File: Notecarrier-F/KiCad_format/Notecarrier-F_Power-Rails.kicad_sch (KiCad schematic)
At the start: 28 parts, among them U10 TPS63020DSJR, U11 MAX17225ELT+, U9 TPS62748YFPT

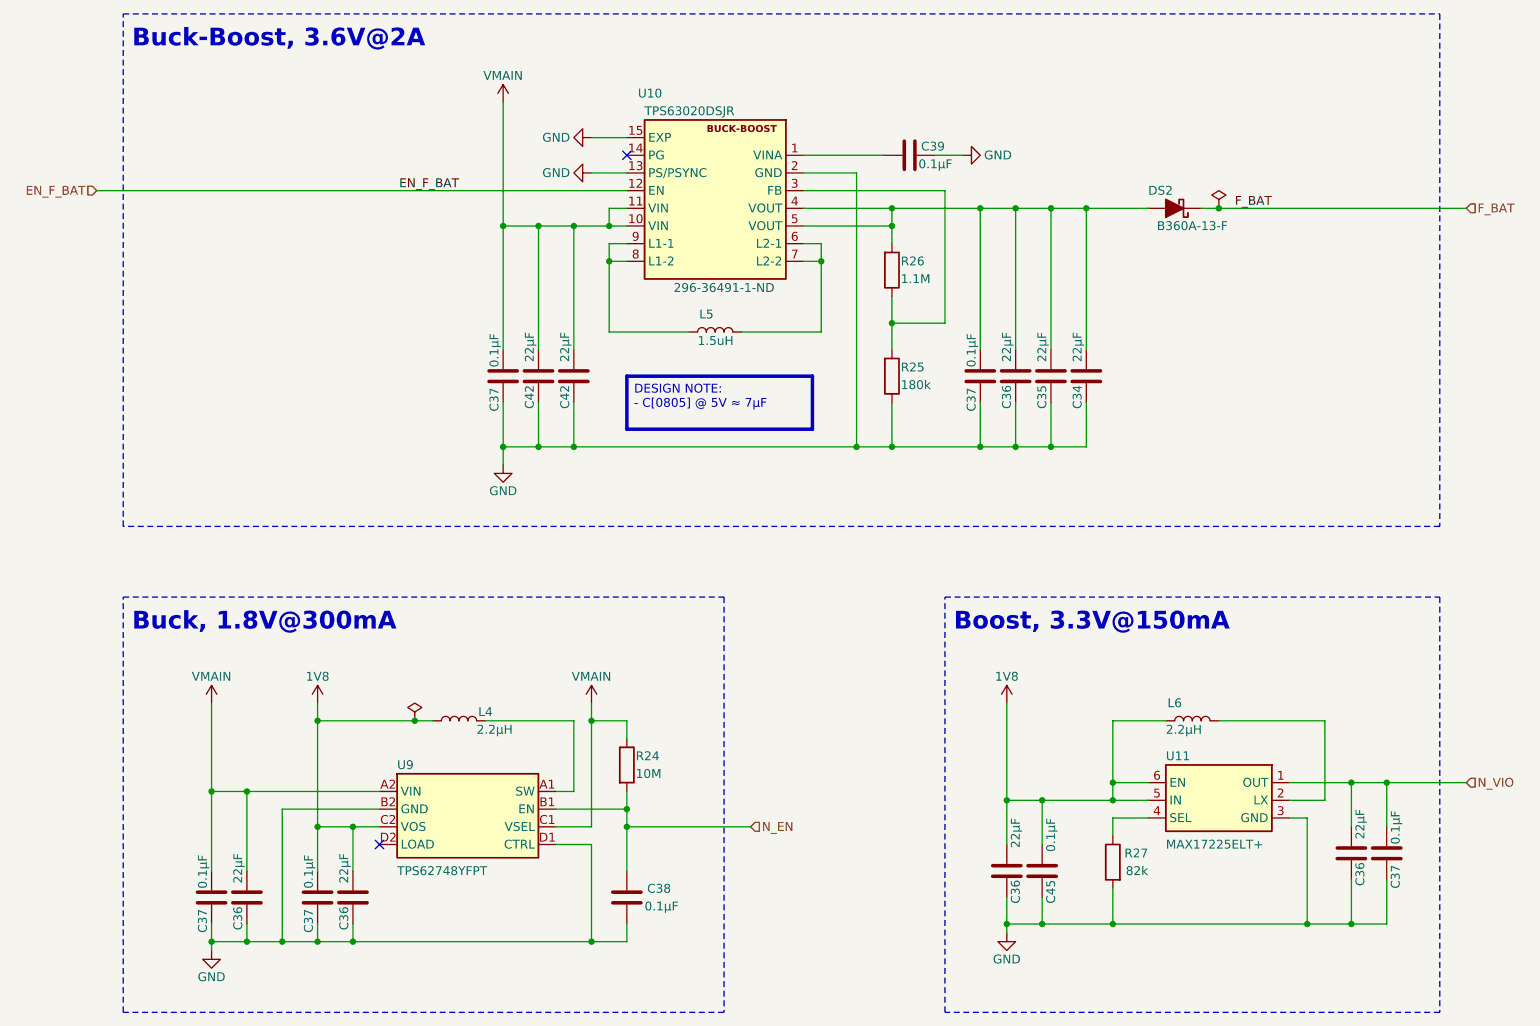
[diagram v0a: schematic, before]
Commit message: Complete first pass PCB rev B.
See README for details. Ready to start Validation.
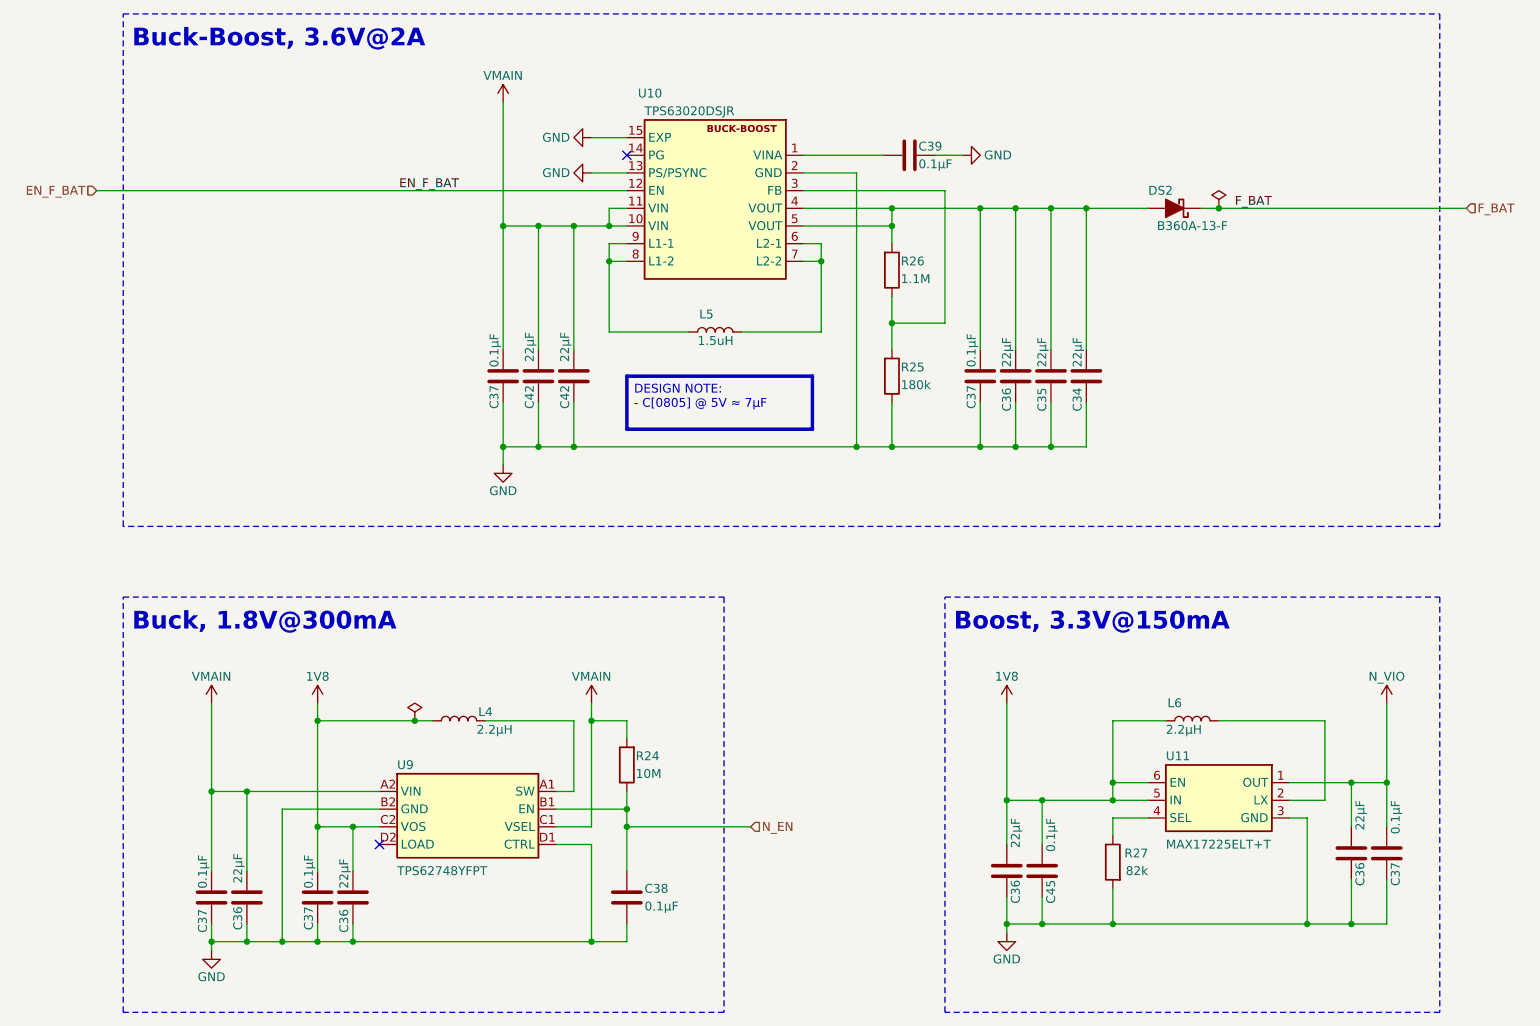
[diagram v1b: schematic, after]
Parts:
- C34, C35, C36: footprint blues-kicad-lib:CAP FILM 0805 -> blues-kicad-lib:C-0805_Fv1.2; Design Description (none) -> Capacitor ceramic 22u ±10% X5R 16V 0805; Design MPN (none) -> N/A; Design Manufacturer (none) -> N/A; MPN (none) -> CL21A226MOQNNNE; Mfr Description (none) -> Cap Ceramic 22uF 16V X5R 20% SMD 0805 85°C Embossed Plastic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; Order Code CL21A226MOQNNNE -> (none); Part Number CL21A226MOQNNNE -> (none); Supplier Avnet -> (none)
- C37, C38, C39, C45: footprint blues-kicad-lib:CAP 0402_1005 -> blues-kicad-lib:C-0402_Fv1.2; Datasheet 2 (none) -> http://datasheet.octopart.com/CL05B104KO5NNNC-Samsung-Elect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; Datasheet 3 (none) -> https://datasheet.octopart.com/GRM155R71C104KA88D-Murata-da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; Design Description (none) -> Capacitor ceramic 100n ±10% X7R 16V 0402; Design MPN (none) -> N/A; Design Manufacturer (none) -> N/A; Design Order Code (none) -> 490-3261-1-ND; Design Supplier (none) -> Digi-Key; MPN (none) -> CC0402KRX7R7BB104; MPN 2 (none) -> CL05B104KO5NNNC; MPN 3 (none) -> GRM155R71C104KA88D; Manufacturer Samsung -> Yageo; Manufacturer 2 (none) -> Samsung; Manufacturer 3 (none) -> Murata; Mfr Description (none) -> 0402 0.1 uF 16 V ±10 % Tolerance X7R SMT Multilayer Ceramic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; Mfr Description 2 (none) -> Ceramic capacitor SMD-0402 100nF /16V X7R# K +-10%, Samsung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; Mfr Description 3 (none) -> Multilayer Ceramic Capacitor, 0.1 uF, 16 V, ± 10%, X7R, 040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; Order Code 187-CL05B104KO5NNNC -> (none); Part Number CL05B104KO5NNNC -> (none); Supplier Farnell -> (none)
- C42: footprint blues-kicad-lib:CAP 0603_1608 -> blues-kicad-lib:C-0805_Fv1.2; Design Description (none) -> Capacitor ceramic 22u ±10% X5R 16V 0805; Design MPN (none) -> N/A; Design Manufacturer (none) -> N/A; MPN (none) -> CL21A226MOQNNNE; Manufacturer (none) -> Samsung; Mfr Description (none) -> Cap Ceramic 22uF 16V X5R 20% SMD 0805 85°C Embossed Plastic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
- DS2: footprint (none) -> blues-kicad-lib:DO-214AC SMA_Fv1.2; symbol Device:D_Schottky_Filled -> blues-kicad-lib:D_Schottky_Filled_Swapped; Design Description (none) -> Schottky Diode B360-13-F 60V/3A; Design MPN (none) -> B360A-13-F; Design Manufacturer (none) -> Diodes Inc; Design Order Code (none) -> B360A-FDICT-ND; Design Supplier (none) -> Digi-Key; MPN (none) -> B360A-13-F; Manufacturer (none) -> Diodes Inc.; Mfr Description (none) -> Rectifier Diode, Schottky, 1 Phase, 1 Element, 3A, 60V V(RR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
- L4: footprint blues-kicad-lib:1285AS-H-2R2M=P2-INDC2016X100N -> blues-kicad-lib:1285AS-H-2R2M=P2-INDC2016X100N_Fv1.2; Design Description (none) -> FIXED IND 2.2UH 1.5A 204MOHM SMD; Design MPN (none) -> 1285AS-H-2R2M=P2; Design Manufacturer (none) -> Murata Electronics; Design Order Code (none) -> 490-10600-1-ND; Design Supplier (none) -> Digi-Key; MPN (none) -> 1285AS-H-2R2M=P2; Mfr Description (none) -> 2.2µH Shielded Wirewound Inductor 1.5A 204mOhm Max 0805 (20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; Order Code 490-10600-1-ND -> (none); Part Number 1285AS-H-2R2M=P2 -> (none); Supplier Digi-Key -> (none)
- L5: footprint blues-kicad-lib:VCHA042A-1R5MS6 -> blues-kicad-lib:VCHA042A-1R5MS6_Fv1.2; Design Description (none) -> Fixed Ind 1.5UH 7.3A 15.4 Mohm; Design MPN (none) -> VCHA042A-1R5MS6; Design Manufacturer (none) -> Cyntec; Design Order Code (none) -> 2037-VCHA042A-1R5MS6CT-ND; Design Supplier (none) -> Digi-Key; MPN (none) -> VCHA042A-1R5MS6; Mfr Description (none) -> Fixed Ind 1.5UH 7.3A 15.4MOHM Sm; Order Code 2037-VCHA042A-1R5MS6CT-ND -> (none); Part Number VCHA042A-1R5MS6 -> (none); Supplier Digi-Key -> (none)
- L6: footprint blues-kicad-lib:IND_XFL4020-222MEC -> blues-kicad-lib:IND_XFL4020-222MEC_Fv1.2; Design Description (none) -> Power Inductors - SMD 2.2Uh Shld 8A 23.5mOhms AECQ2; Design MPN (none) -> XFL4020-222MEC; Design Manufacturer (none) -> Coilcraft; Design Order Code (none) -> 994-XFL4020-222MEC; Design Supplier (none) -> Mouser; MPN (none) -> XFL4020-222MEC; Mfr Description (none) -> Inductor Power Shielded Wirewound 2.2uH 20% 1MHz 8A 0.0235O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; Order Code XFL4020-222MEC -> (none); Part Number XFL4020-222MEC -> (none)
- R24: footprint blues-kicad-lib:RES 0402_1005 -> blues-kicad-lib:R-0402_Fv1.2; Datasheet 2 (none) -> https://datasheet.octopart.com/AC0402FR-0710ML-Yageo-datash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; Design Description (none) -> Resistor 10M ±1% 0402; Design MPN (none) -> N/A; Design Manufacturer (none) -> N/A; Design Order Code (none) -> RC0402FR-0710ML; Design Supplier (none) -> Digi-Key; MPN (none) -> RC0402FR-0710ML; MPN 2 (none) -> AC0402FR-0710ML; Manufacturer 2 (none) -> Yageo; Mfr Description (none) -> Res General Purpose Thick Film 0402 10M Ohm 1% 1/16W ±100pp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; Mfr Description 2 (none) -> Res Thick Film 0402 10M Ohm 1% 0.063W(1/16W) ±100ppm/C Pad 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; Order Code 311-10MJRCT-ND -> (none); Part Number RC0402JR-0710ML -> (none); Supplier Digi-Key -> (none)
- R25: footprint blues-kicad-lib:RES 0402_1005 -> blues-kicad-lib:R-0402_Fv1.2; Design Description (none) -> Resistor 180k ±1% 0402; Design MPN (none) -> N/A; Design Manufacturer (none) -> N/A; MPN (none) -> RC0402FR-07180KL; Mfr Description (none) -> Res Thick Film 0402 180K Ohm 1% 1/16W +/-100ppm/ßC Molded S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; Order Code 311-180KLRTR-ND -> (none); Part Number RC0402FR-07180KL -> (none); Supplier Digi-Key -> (none)
- R26: footprint blues-kicad-lib:RES 0402_1005 -> blues-kicad-lib:R-0402_Fv1.2; Datasheet 2 (none) -> https://datasheet.octopart.com/RC0402FR-071M1L-Yageo-datash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; Design Description (none) -> Resistor 1M1 ±1% 0402; Design MPN (none) -> N/A; Design Manufacturer (none) -> N/A; Design Order Code (none) -> 13-RC0402FR-071M1LCT-ND; Design Supplier (none) -> Digi-Key; MPN (none) -> AC0402FR-071M1L; MPN 2 (none) -> RC0402FR-071M1L; Manufacturer 2 (none) -> Yageo; Mfr Description (none) -> Res Thick Film 0402 1.1M Ohm 1% 0.063W(1/16W) ±100ppm/C Pad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; Mfr Description 2 (none) -> SMD Chip Resistor, 1.1 MOhm, ± 1%, 63 mW, 0402 [1005 Metric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; Order Code YAG5647CT-ND -> (none); Part Number AC0402FR-071M1L -> (none); Supplier Digi-Key -> (none)
- R27: footprint blues-kicad-lib:RES 0402_1005 -> blues-kicad-lib:R-0402_Fv1.2; Datasheet 2 (none) -> http://datasheet.octopart.com/RC0402FR-0782KL-Yageo-datashe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; Datasheet 3 (none) -> http://datasheet.octopart.com/RMCF0402FT82K0-Stackpole-Elec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; Design Description (none) -> Resistor 82k ±1% 0402; Design MPN (none) -> RC0402FR-0782KL; Design Manufacturer (none) -> Yageo; Design Order Code (none) -> 311-82.0KLRCT-ND; Design Supplier (none) -> Digi-key; MPN (none) -> CRCW040282K0FKED; MPN 2 (none) -> RC0402FR-0782KL; MPN 3 (none) -> RMCF0402FT82K0; Manufacturer Stackpole Electronics -> Vishay; Manufacturer 2 (none) -> Yageo; Manufacturer 3 (none) -> Stackpole Electronics; Mfr Description (none) -> Res Thick Film 0402 82K Ohm 1% 1/16W ±100ppm/°C Molded SMD 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; Mfr Description 2 (none) -> Res Thick Film 0402 82K Ohm 1% 0.063W(1/16W) ±100ppm/C Pad 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; Mfr Description 3 (none) -> Res Thick Film 0402 82K Ohm 1% 0.063W(1/16W) ±100ppm/C Pad 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; Order Code RMCF0402FT82K0CT-ND -> (none); Part Number RMCF0402FT82K0 -> (none); Supplier Digi-Key -> (none)
- U10: footprint blues-kicad-lib:TI PVSON-14 DSJ -> blues-kicad-lib:TI PVSON-14 DSJ_Fv1.2; Datasheet 2 (none) -> https://octopart.com/opatz8j6/c1?t=F5MXvDztptQJYCfOaNqYA5YH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; Design Description (none) -> I.C. DC/DC CONVERTER TPS63020DSJR TEXAS VSON14 SMT; Design MPN (none) -> TPS63020DSJR; Design Manufacturer (none) -> Texas Instruments; Design Order Code (none) -> 296-36491-1-ND; Design Supplier (none) -> Digi-Key; MPN (none) -> TPS63020DSJR; MPN 2 (none) -> TPS63020DSJT; Manufacturer 2 (none) -> Texas Instruments; Mfr Description (none) -> High Efficiency Single Inductor Buck-Boost Converter with 4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; Mfr Description 2 (none) -> High Efficiency Single Inductor Buck-Boost Converter with 4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; Order Code 296-36491-1-ND -> (none); Part Number TPS63020DSJR -> (none); Supplier Digi-Key -> (none)
- U11: value MAX17225ELT+ -> MAX17225ELT+T; footprint blues-kicad-lib:MAX17225ELT+UDFN -> blues-kicad-lib:MAX17225ELT+UDFN_Fv1.2; Design Description (none) -> IC REG BOOST ADJ 1A NANO 6UDFN; Design MPN (none) -> MAX17225ELT+; Design Manufacturer (none) -> Maxim; Design Order Code (none) -> MAX17225ELT+ -ND; Design Supplier (none) -> Digi-Key; MPN (none) -> MAX17225ELT+T; Manufacturer Maxim -> Maxim Integrated; Mfr Description (none) -> nanoPower Boost Converter that Extends Battery Life and Red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; Order Code MAX17225ELT+ -ND -> (none); Part Number MAX17225ELT+ -> (none); Supplier Digi-Key -> (none)
- U9: footprint blues-kicad-lib:TPS62748YFPT-DSBGA4x2 -> blues-kicad-lib:TPS62748YFPT-DSBGA4x2_Fv1.2; Datasheet 2 (none) -> https://octopart.com/click/track?ai=8983&ct=datasheets&sig=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; Design Description (none) -> IC REG BUCK PROG 300MA 8DSBGA; Design MPN (none) -> TPS62748YFPT; Design Manufacturer (none) -> Texas Instruments; Design Order Code (none) -> 296-43000-1-ND; Design Supplier (none) -> Digi-Key; MPN (none) -> TPS62748YFPR; MPN 2 (none) -> TPS62748YFPT; Manufacturer 2 (none) -> Texas Instruments; Mfr Description (none) -> High-efficiency Buck Converter with Ultra-low Quiescent Cur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; Mfr Description 2 (none) -> Conv DC-DC 2.15V to 5.5V Step Down Single-Out 1.2V/1.8V 0.3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; Order Code TPS62748YFPT -> (none); Part Number TPS62748YFPT -> (none); Supplier Texas Instruments -> (none)
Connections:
- net 1V8: now also C36.1, C37.2; no longer C36.2, C37.1
- net F_BAT: now also DS2.2 (K); no longer DS2.1 (K)
- net GND: now also C34.2, C35.2, C36.2, C36.2, C37.1, C37.1, C37.1, C37.1, C38.2, C39.1; no longer C34.1, C35.1, C36.1, C36.1, C37.2, C37.2, C37.2, C37.2, C38.1, C39.2
- net N_EN: now also C38.1, R24.1; no longer C38.2, R24.2
- net N_VIO: now also C37.2; no longer C37.1
- net VMAIN: now also C37.2, R24.2; no longer C37.1, R24.1
- net at U10.1 (VINA): now also C39.2; no longer C39.1
- new net: C34.1, C35.1, C36.1, C37.2, DS2.1 (A), R26.2, U10.4 (VOUT), U10.5 (VOUT)
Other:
- moved on the sheet: C34, C35, C36, C37, C38, C39, R24

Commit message: Apply cosmetic tweaks from Validation activity.
- Remove 4 way junction.
- Remove off-grid connections.
- Correct visible component values
- Add missing design notes.
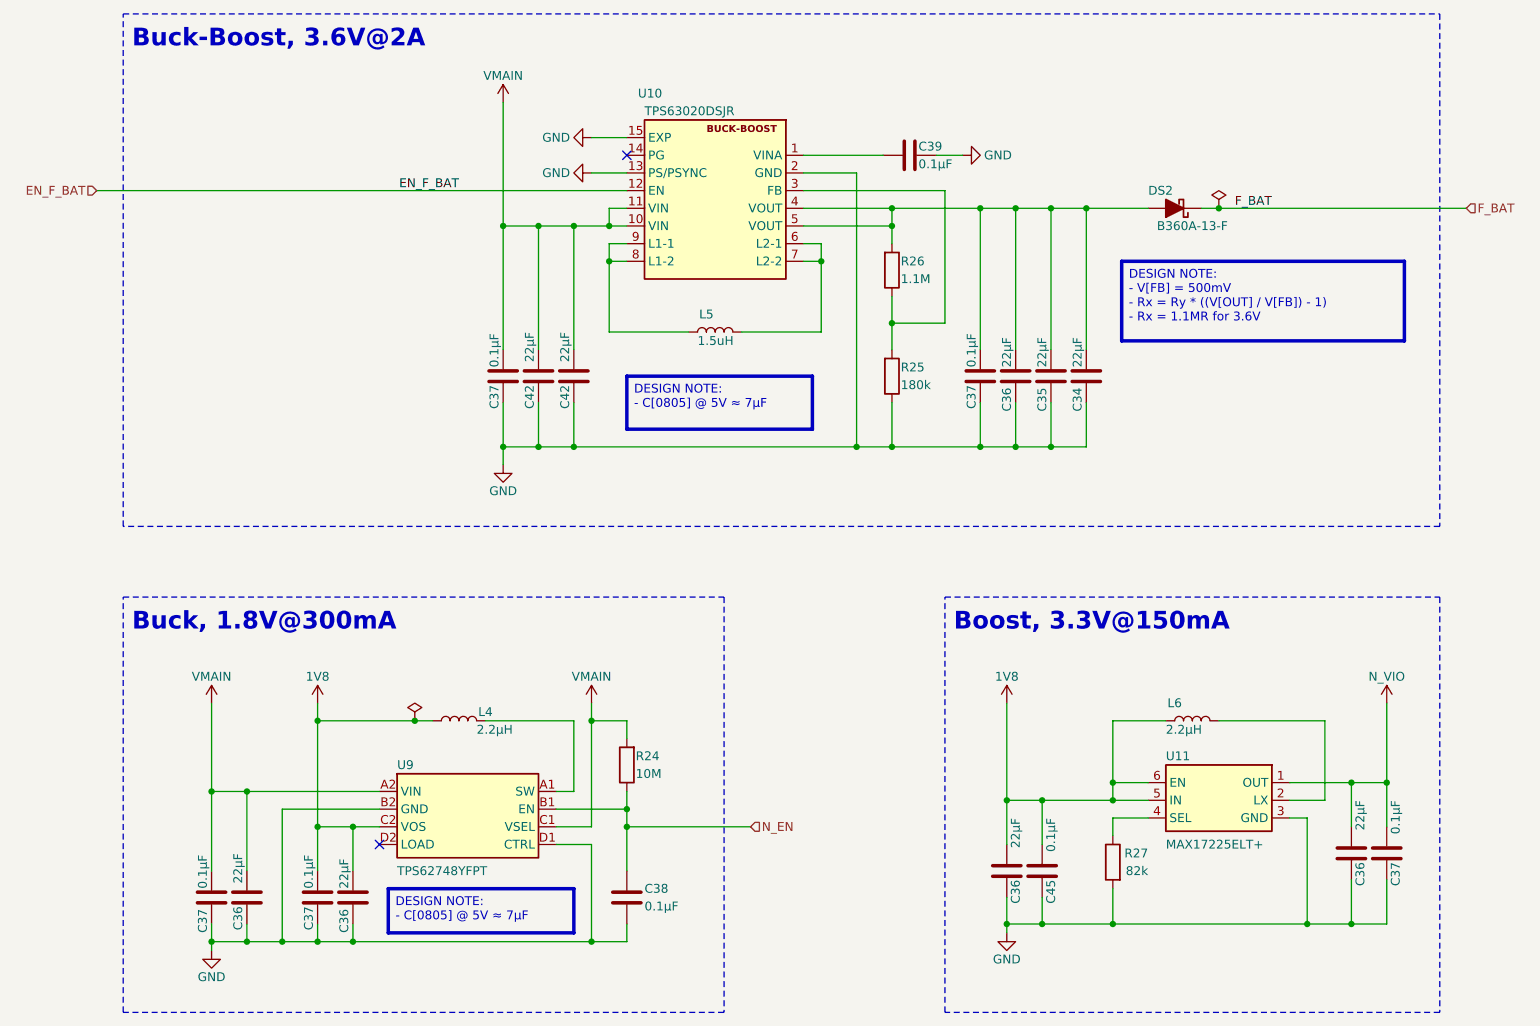
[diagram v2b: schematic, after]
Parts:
- U11: value MAX17225ELT+T -> MAX17225ELT+
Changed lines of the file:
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@@
+    (effects (font (size 1.27 1.27) (color 0 0 0 1)) (justify left top))
+  )
+  (text_box "DESIGN NOTE:\n- C[0805] @ 5V ≈ 7µF"
+    (at 93.98 147.32 0) (size 26.67 6.35)
+    (stroke (width 0.5) (type default) (color 194 0 0 1))
+    (fill (type none))
+    (effects (font (size 1.27 1.27) (color 0 0 0 1)) (justify left top))
+  )
+  (text_box "DESIGN NOTE:\n- V[FB] = 500mV\n- Rx = Ry * ((V[OUT] / V[FB]) - 1)\n- Rx = 1.1MR for 3.6V"
+    (at 199.39 57.15 0) (size 40.64 11.43)
+    (stroke (width 0.5) (type default) (color 194 0 0 1))
+    (fill (type none))
     (effects (font (size 1.27 1.27) (color 0 0 0 1)) (justify left top))
   )
@@
       (effects (font (size 1.27 1.27)) (justify right))
     )
-    (property "Value" "MAX17225ELT+T" (at 205.74 140.97 0)
+    (property "Value" "MAX17225ELT+" (at 205.74 140.97 0)
       (effects (font (size 1.27 1.27)) (justify right))
     )

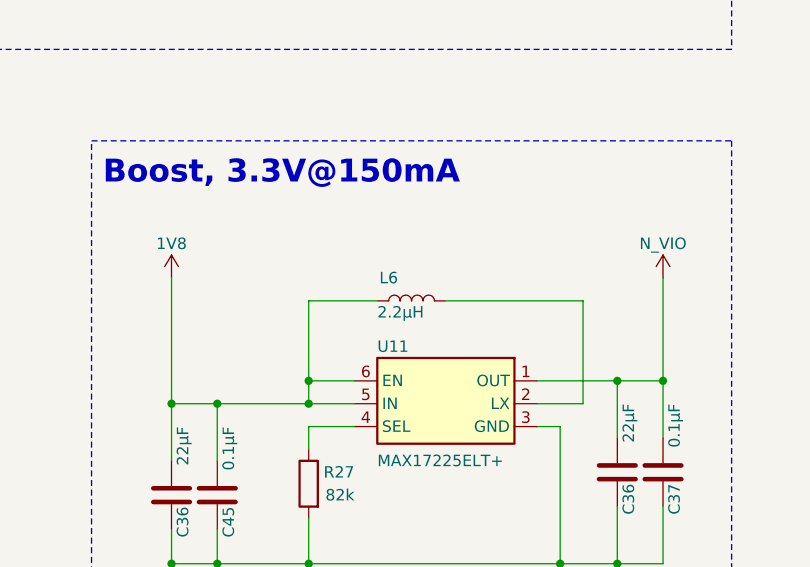
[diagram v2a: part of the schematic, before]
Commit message: Complete validation.
A few minor touch-ups to fills, polygons and DRC exclusions.
Most significantly, re-assigned “GND” net to most (all?) of the weird-no-fill-via footprints, which got unassigned in a previous update-from-libraries. Also locked them all to reduce likely of losing the assignments in future, but it’s a hack so not sure it will stick - be wary. Also locked the M2 footprint because I overrode the fill settings on a few pads to “none” to prevent thermal reliefs being generated.
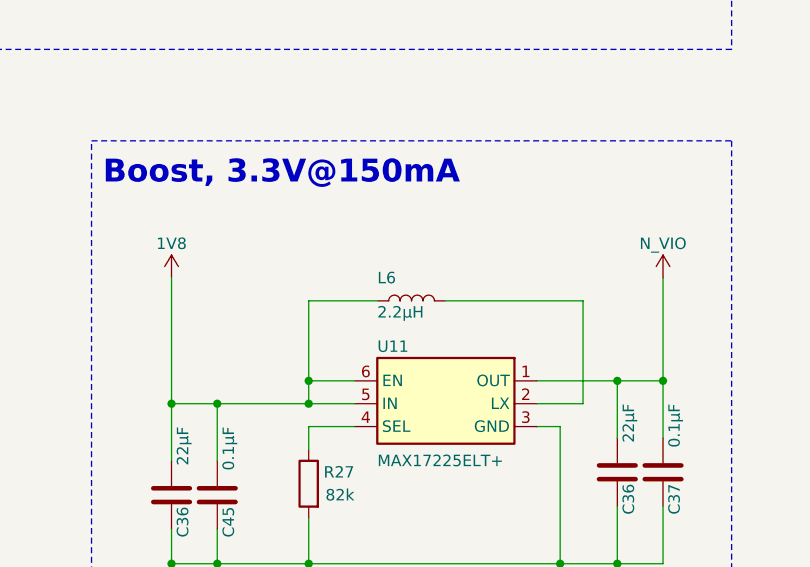
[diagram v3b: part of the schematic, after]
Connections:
- net 1V8: now also L6.2; no longer L6.1
- net at U11.2 (LX): now also L6.1; no longer L6.2
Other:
- moved on the sheet: L6
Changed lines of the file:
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@@
     )
   )
-  (symbol (lib_id "Device:L") (at 209.55 123.19 90) (unit 1)
+  (symbol (lib_id "Device:L") (at 209.55 123.19 270) (mirror x) (unit 1)
     (in_bom yes) (on_board yes) (dnp no)
-    (property "Reference" "L6" (at 207.01 120.65 90)
-      (effects (font (size 1.27 1.27)))
+    (property "Reference" "L6" (at 205.74 120.65 90)
+      (effects (font (size 1.27 1.27)) (justify left))
     )
     (property "Value" "2.2µH" (at 205.74 124.46 90)
-      (effects (font (size 1.27 1.27)) (justify right))
+      (effects (font (size 1.27 1.27)) (justify left))
     )
     (property "Footprint" "blues-kicad-lib:IND_XFL4020-222MEC_Fv1.2" (at 209.55 123.19 0)
